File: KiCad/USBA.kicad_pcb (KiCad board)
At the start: 2 copper layers, 19 x 20.2 mm, 16 parts, among them J1 USB_A, SW1 SW_Push, U1 ESP32-WROOM-32, U2 FT231XQ, U4 LMR16006YQ3

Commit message: Tweak
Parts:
- added U3: QR, RevK:QR-GENERIC, B.Cu at (121.5, 126.0)
- Logo1: moved to F.Cu
- moved Logo1 19.4 mm to (118.6, 107.8), turned to 90 degrees
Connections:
- U1 pad 11: Net-(U1-Pad11) -> Net-(SW1-Pad1)
- U1 pad 31: Net-(SW1-Pad1) -> Net-(U1-Pad31)
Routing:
- net Net-(SW1-Pad1): track 31.1 -> 15.2 mm, vias 3 -> 1
- net GND: track 75.3 -> 70.6 mm, vias 10 -> 9
- net O: track 26.2 -> 24.6 mm

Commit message: New QR
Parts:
- U3: footprint RevK:QR-GENERIC -> RevK:QR-HA
- moved Logo1 0.60 mm to (118.6, 107.2)
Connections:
- U1 pad 10: G -> B
- U1 pad 11: Net-(SW1-Pad1) -> G
- U1 pad 8: R -> Net-(SW1-Pad1)
- U1 pad 9: B -> R
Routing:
- net GND: track 70.6 -> 53.9 mm, vias 9 -> 8
- net Net-(SW1-Pad1): track 15.2 -> 17.6 mm
- net O: track 24.6 -> 26.5 mm
- net R: track 25.3 -> 24.4 mm
- net G: track 22.0 -> 22.5 mm

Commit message: Moved button
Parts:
- moved C2 13.8 mm to (117.7, 102.3), turned to 90 degrees
- moved Logo1 8.70 mm to (126.8, 110.1)
- moved SW1 4.85 mm to (121.5, 116.0), turned to 0 degrees
- moved U2 4.72 mm to (117.9, 108.4), turned to 0 degrees
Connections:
- U1 pad 10: B -> Net-(U1-Pad10)
- U1 pad 11: G -> Net-(U1-Pad11)
- U1 pad 12: Net-(U1-Pad12) -> Net-(SW1-Pad1)
- U1 pad 30: CHARGER -> Net-(U1-Pad30)
- U1 pad 33: Net-(U1-Pad33) -> G
- U1 pad 36: Net-(U1-Pad36) -> B
- U1 pad 37: Net-(U1-Pad37) -> R
- U1 pad 6: Net-(U1-Pad6) -> CHARGER
- U1 pad 8: Net-(SW1-Pad1) -> Net-(U1-Pad8)
- U1 pad 9: R -> Net-(U1-Pad9)
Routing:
- net R: track 24.4 -> 4.09 mm
- net O: track 26.5 -> 7.02 mm, vias 3 -> 1
- net B: track 23.1 -> 4.09 mm
- net GND: track 53.9 -> 36.0 mm, vias 8 -> 7
- net G: track 22.5 -> 7.28 mm
- net GPIO0: track 8.30 -> 22.0 mm
- net CHARGER: track 3.82 -> 16.7 mm
- net EN: track 27.6 -> 15.8 mm
- net D-: track 15.8 -> 18.9 mm
- net I: track 9.79 -> 6.73 mm
- net VBUS: track 31.5 -> 28.4 mm
- net D+: track 14.9 -> 17.6 mm
- net Net-(SW1-Pad1): track 17.6 -> 15.0 mm, vias 1 -> 2

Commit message: As ordered
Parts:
- moved C2 0.50 mm to (117.2, 102.3)
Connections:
- U1 pad 16: Net-(U1-Pad16) -> GND
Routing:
- net GND: track 36.0 -> 44.5 mm
- net Net-(C2-Pad1): track 13.5 -> 15.1 mm
- net EN: track 15.8 -> 15.2 mm
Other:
- board text added: "^HA"

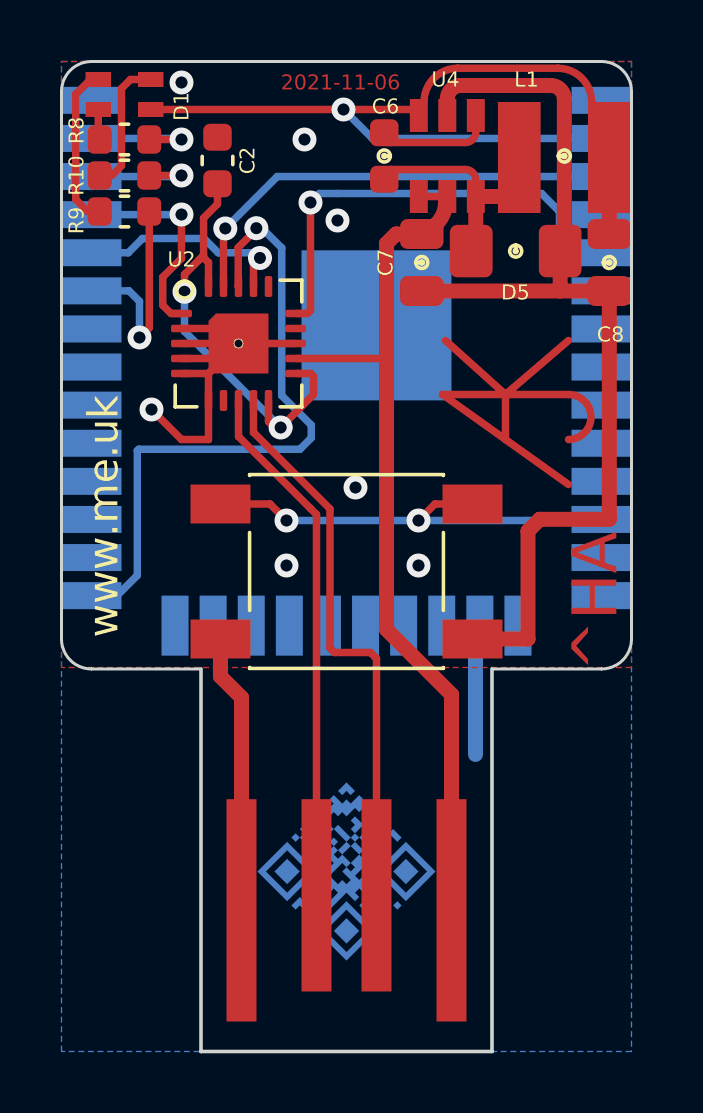
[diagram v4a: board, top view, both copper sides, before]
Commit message: Revised USB plug
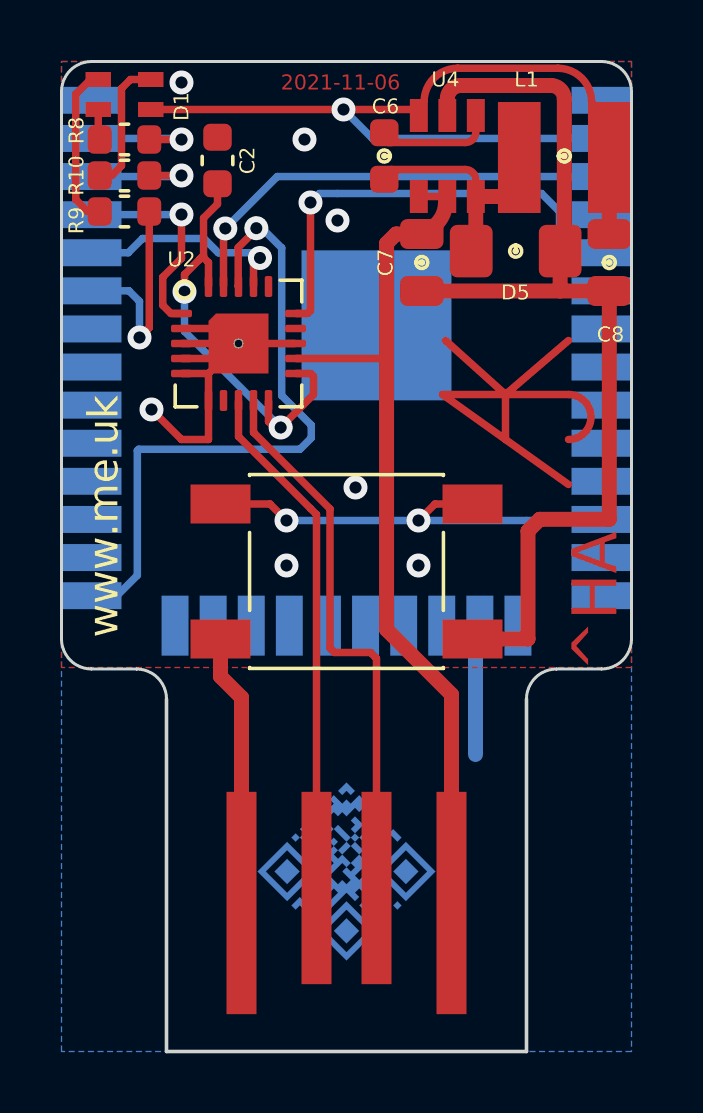
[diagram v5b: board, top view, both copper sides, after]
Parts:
- moved J1 1.00 mm to (121.5, 132.0)
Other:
- board size 19 x 20.2 mm -> 19 x 21.2 mm

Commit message: Revised version
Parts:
- U4: renamed from U3; moved to F.Cu
- moved U4 17.0 mm to (127.1, 110.0), turned to 0 degrees
- moved Logo1 14.2 mm to (114.3, 116.9), turned to 180 degrees
- renumbered C2 to C1, C6 to C2, C7 to C3, C8 to C4, D5 to D2, R8 to R1, R9 to R2, R10 to R3, U4 to U3
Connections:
- U1 pad 16: GND -> Net-(U1-Pad16)
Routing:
- net GND: track 44.5 -> 47.9 mm
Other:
- board text added: "2021-11-10"
- board text added: "^BS"
- board text removed: "2021-11-06"

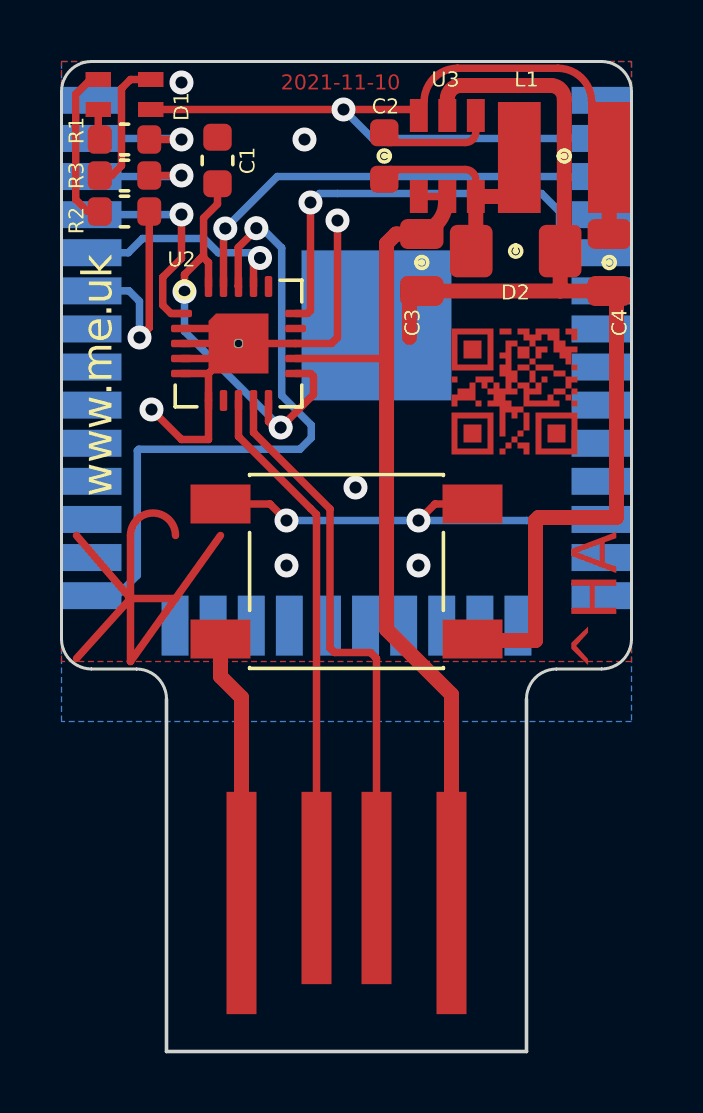
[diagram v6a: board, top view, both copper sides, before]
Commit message: Revised plug outline
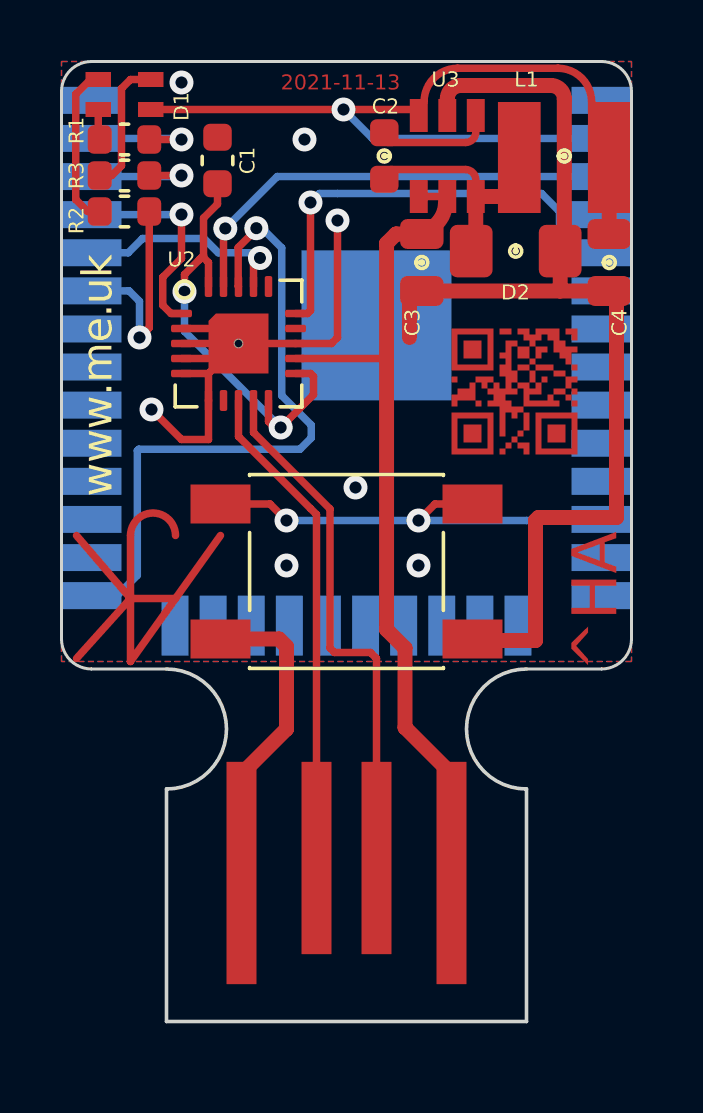
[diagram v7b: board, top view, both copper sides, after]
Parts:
- moved J1 1.00 mm to (121.5, 131.0)
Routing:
- net VBUS: track 28.4 -> 27.2 mm
- net GND: track 47.9 -> 49.1 mm
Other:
- board size 19 x 21.2 mm -> 19 x 20.2 mm
- board text added: "2021-11-13"
- board text removed: "2021-11-10"

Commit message: Kicad 6
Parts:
- moved Logo1 0.23 mm to (114.5, 117.1)
- moved SW1 0.10 mm to (121.5, 116.1)
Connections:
- U1 pad 10: Net-(U1-Pad10) -> unconnected-(U1-Pad10)
- U1 pad 11: Net-(U1-Pad11) -> unconnected-(U1-Pad11)
- U1 pad 13: Net-(U1-Pad13) -> unconnected-(U1-Pad13)
- U1 pad 14: Net-(U1-Pad14) -> unconnected-(U1-Pad14)
- U1 pad 16: Net-(U1-Pad16) -> unconnected-(U1-Pad16)
- U1 pad 17: Net-(U1-Pad17) -> unconnected-(U1-Pad17)
- U1 pad 18: Net-(U1-Pad18) -> unconnected-(U1-Pad18)
- U1 pad 19: Net-(U1-Pad19) -> unconnected-(U1-Pad19)
- U1 pad 20: Net-(U1-Pad20) -> unconnected-(U1-Pad20)
- U1 pad 21: Net-(U1-Pad21) -> unconnected-(U1-Pad21)
- U1 pad 22: Net-(U1-Pad22) -> unconnected-(U1-Pad22)
- U1 pad 23: Net-(U1-Pad23) -> unconnected-(U1-Pad23)
- U1 pad 24: Net-(U1-Pad24) -> unconnected-(U1-Pad24)
- U1 pad 26: Net-(U1-Pad26) -> unconnected-(U1-Pad26)
- U1 pad 27: Net-(U1-Pad27) -> unconnected-(U1-Pad27)
- U1 pad 28: Net-(U1-Pad28) -> unconnected-(U1-Pad28)
- U1 pad 29: Net-(U1-Pad29) -> unconnected-(U1-Pad29)
- U1 pad 30: Net-(U1-Pad30) -> unconnected-(U1-Pad30)
- U1 pad 31: Net-(U1-Pad31) -> unconnected-(U1-Pad31)
- U1 pad 32: Net-(U1-Pad32) -> unconnected-(U1-Pad32)
- U1 pad 4: Net-(U1-Pad4) -> unconnected-(U1-Pad4)
- U1 pad 5: Net-(U1-Pad5) -> unconnected-(U1-Pad5)
- U1 pad 7: Net-(U1-Pad7) -> unconnected-(U1-Pad7)
- U1 pad 8: Net-(U1-Pad8) -> unconnected-(U1-Pad8)
- U1 pad 9: Net-(U1-Pad9) -> unconnected-(U1-Pad9)
- U2 pad 14: Net-(U2-Pad14) -> unconnected-(U2-Pad14)
- U2 pad 16: Net-(U2-Pad16) -> unconnected-(U2-Pad16)
- U2 pad 7: Net-(U2-Pad7) -> unconnected-(U2-Pad7)
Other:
- net class Default removed
